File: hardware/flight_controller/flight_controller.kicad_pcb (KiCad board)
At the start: 2 copper layers, 156.2 x 48.3 mm, 20 parts, among them J1 Conn_02x04_Odd_Even, J2 Conn_01x03, J3 Conn_01x03, J4 Conn_01x03, J5 Conn_01x03, J6 Conn_01x05, J7 Conn_01x03, U1 Teensy3.6, U2 Logic_Level_Converter, U3 Logic_Level_Converter

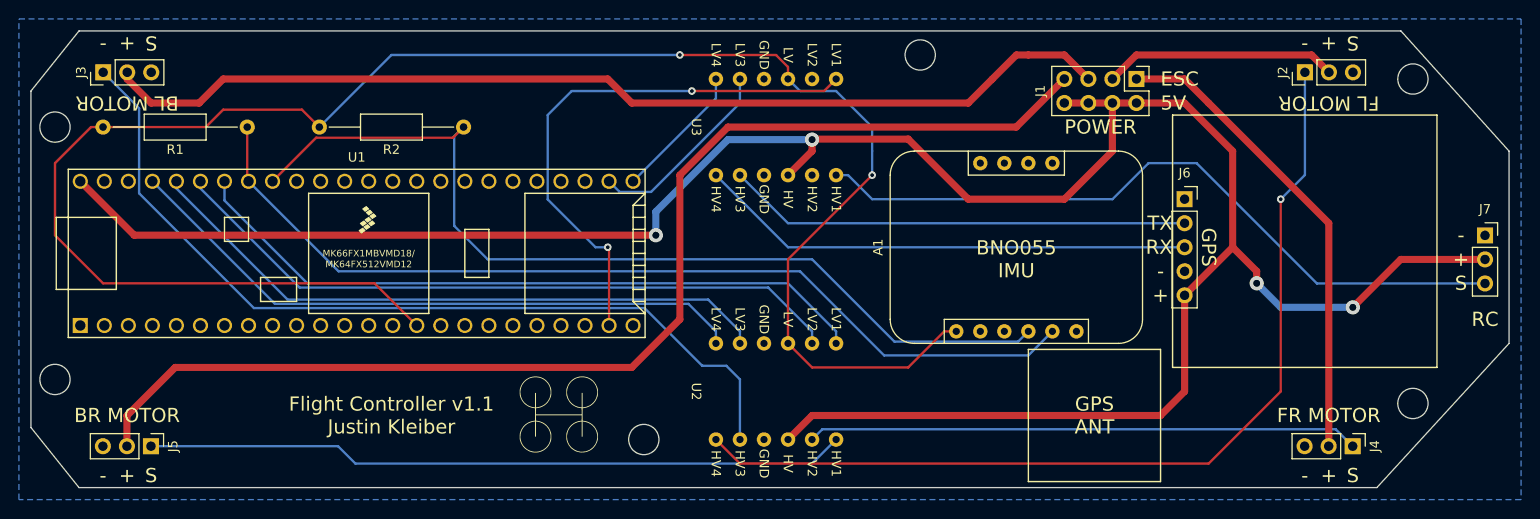
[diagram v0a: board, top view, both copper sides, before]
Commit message: Wired up the quadcopter with v1.1 and tried to fly it. Control loops still need tuning, but auto-stop works
Begins updated v1.2 PCB (just errata of v1.1 for now) and need to improve simulation with initial system ID

Weighed drone and it weighs 1 kg (1001 g)
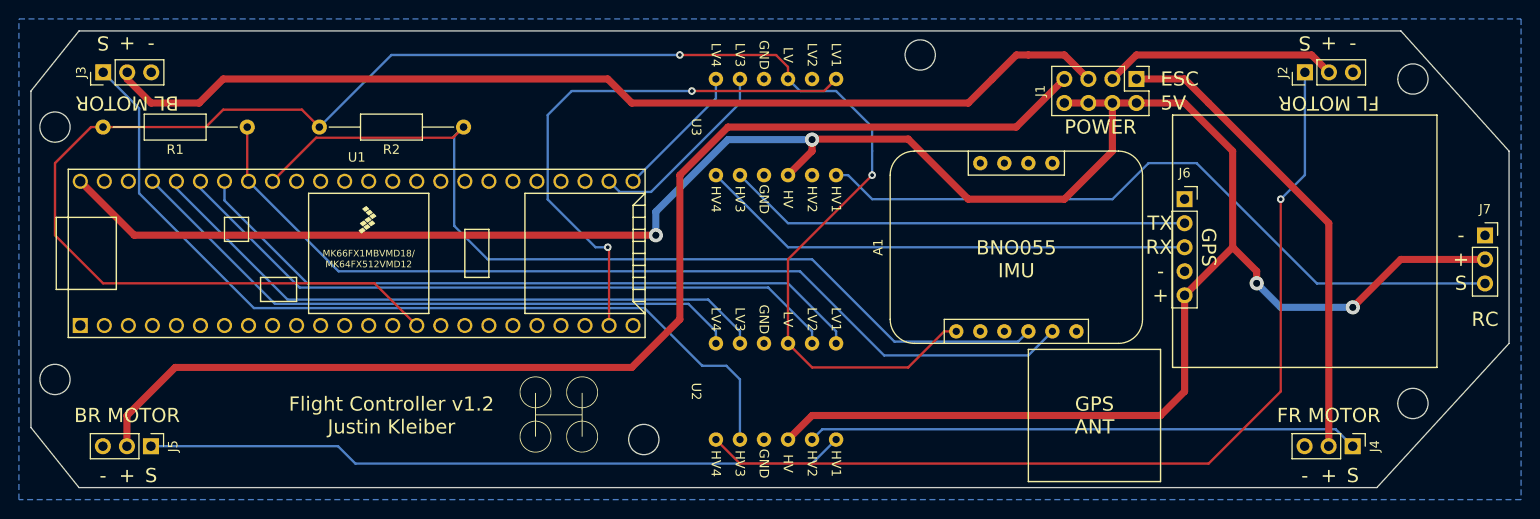
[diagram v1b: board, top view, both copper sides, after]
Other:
- board text added: "Flight Controller v1.2 Justin Kleiber"
- board text removed: "Flight Controller v1.1 Justin Kleiber"
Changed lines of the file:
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@@
       (xy 241.3 83.82)
     ) (layer "Edge.Cuts") (width 0.1) (fill none))
-  (gr_text "S" (at 109.235 85.09 180) (layer "F.SilkS")
+  (gr_text "S" (at 104.14 85.09 180) (layer "F.SilkS")
     (effects (font (size 1.5 1.5) (thickness 0.3)))
   )
@@
     (effects (font (size 1.5 1.5) (thickness 0.3)))
   )
-  (gr_text "-" (at 104.155 85.09) (layer "F.SilkS")
+  (gr_text "-" (at 109.22 85.09) (layer "F.SilkS")
     (effects (font (size 1.5 1.5) (thickness 0.3)))
   )
@@
     (effects (font (size 1.5 1.5) (thickness 0.3)) (justify left))
   )
-  (gr_text "S" (at 236.22 85.09 180) (layer "F.SilkS")
+  (gr_text "S" (at 231.14 85.09 180) (layer "F.SilkS")
     (effects (font (size 1.5 1.5) (thickness 0.3)))
   )
@@
     (effects (font (size 1.5 1.5) (thickness 0.3)))
   )
-  (gr_text "-" (at 231.14 85.09) (layer "F.SilkS")
+  (gr_text "-" (at 236.22 85.09) (layer "F.SilkS")
     (effects (font (size 1.5 1.5) (thickness 0.3)))
   )
@@
     (effects (font (size 1.5 1.5) (thickness 0.3)) (justify right))
   )
-  (gr_text "Flight Controller v1.1\nJustin Kleiber" (at 134.62 124.46) (layer "F.SilkS")
+  (gr_text "Flight Controller v1.2\nJustin Kleiber" (at 134.62 124.46) (layer "F.SilkS")
     (effects (font (size 1.5 1.5) (thickness 0.3)))
   )
